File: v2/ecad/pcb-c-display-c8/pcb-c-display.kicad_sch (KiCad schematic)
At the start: 192 parts, among them Q1 AO3401A P-FET high side, Q2 2N7002, Q3 2N7002, Q4 2N7002, Q5 AO3401A P-FET: the e-paper's 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, Q6 Si1308EDL class N-FET (RDS un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, U1 PCA9555PW 0x22: LED sinks, li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, U2 PCA9555PW 0x23: LED sinks, th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, U3 RP2040 panel controller (USB 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, U4 W25Q16JVUXIQ 16 Mbit QSPI fla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, U5 TLV75533PDBV 3.3 V 500 mA LDO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, U6 USBLC6-2SC6, U7 USBLC6-2SC6, U8 USBLC6-2SC6, U9 74LVC1G34 non-inverting buffe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, Y1 12 MHz ABM8-272-T3 (3225): 1 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

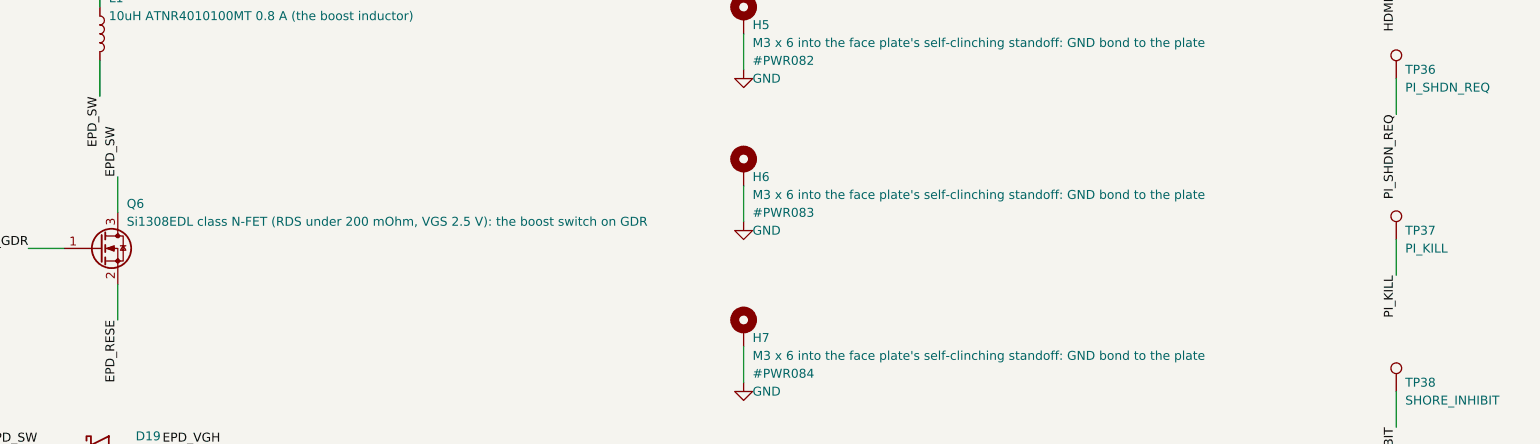
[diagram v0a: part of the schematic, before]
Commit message: chore(ecad): the phase directories' netlists brought current, and the contracts pass 42 of 42 [MESHSAT-862]
check_contracts read every board as MISSING because the netlist beside it in this tree was older than the
schematic beside it: B's by two days, C's by a day, D's and E's by the re-cuts of the 13th. A netlist older
than its schematic is not a netlist of that board, and the check is right to refuse it, so the cross-board
gate has been INCONCLUSIVE rather than passing for as long as those copies have been stale.

Fetched from the phase directories that generated them, schematic and netlist together. ALL CONTRACTS PASS,
42 of 42, the first reading of this gate on seven boards that all exist.
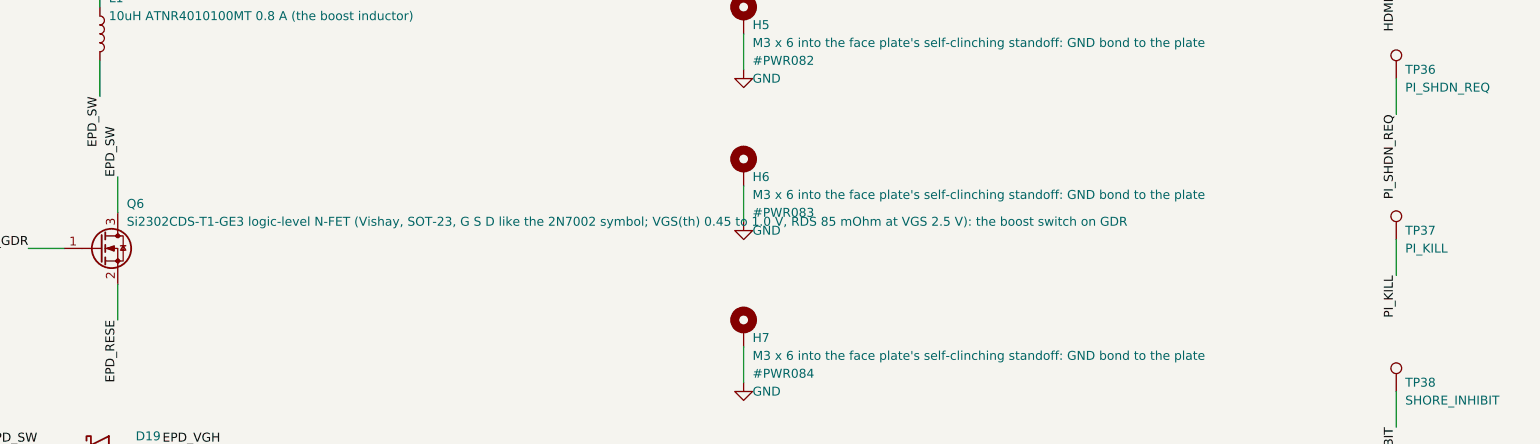
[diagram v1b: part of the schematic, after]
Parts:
- Q6: value Si1308EDL class N-FET (RDS under 200 mOhm, VGS 2.5 V): the boost switch on GDR -> Si2302CDS-T1-GE3 logic-level N-FET (Vishay, SOT-23, G S D like the 2N7002 symbol; VGS(th) 0.45 to 1.0 V, RDS 85 mOhm at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; LCSC C8545 -> C10488
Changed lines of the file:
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@@
 	(symbol (lib_id "Transistor_FET:2N7002") (at 500.38 222.25 0) (unit 1) (exclude_from_sim no) (in_bom yes) (on_board yes) (dnp no) (fields_autoplaced yes)
 		(property "Reference" "Q6" (at 504.19 215.90 0) (effects (font (size 1.27 1.27)) (justify left)))
-		(property "Value" "Si1308EDL class N-FET (RDS under 200 mOhm, VGS 2.5 V): the boost switch on GDR" (at 504.19 218.44 0) (effects (font (size 1.27 1.27)) (justify left)))
+		(property "Value" "Si2302CDS-T1-GE3 logic-level N-FET (Vishay, SOT-23, G S D like the 2N7002 symbol; VGS(th) 0.45 to 1.0 V, RDS 85 mOhm at VGS 2.5 V): the boost switch on GDR" (at 504.19 218.44 0) (effects (font (size 1.27 1.27)) (justify left)))
 		(property "Footprint" "Package_TO_SOT_SMD:SOT-23" (at 500.38 222.25 0) (effects (font (size 1.27 1.27)) (justify left) (hide yes)))
 		(property "Datasheet" "" (at 500.38 222.25 0) (effects (font (size 1.27 1.27)) (justify left) (hide yes)))
 		(property "Description" "" (at 500.38 222.25 0) (effects (font (size 1.27 1.27)) (justify left) (hide yes)))
-		(property "LCSC" "C8545" (at 500.38 222.25 0) (effects (font (size 1.27 1.27)) (justify left) (hide yes)))
+		(property "LCSC" "C10488" (at 500.38 222.25 0) (effects (font (size 1.27 1.27)) (justify left) (hide yes)))
 		(pin "1")
 		(pin "3")

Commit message: feat(c): C17 cut, the first C deliverable: 0 hard, 0 unrouted, check ALL PASS, 1 of 1 rails MET, netlist 852 of 852, verify_deliverable 36 of 36 [MESHSAT-862]
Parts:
- CAM_H1, CAM_H2: now left out of the parts list
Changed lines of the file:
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@@
 		(instances (project "pcb-c-display" (path "/d6380e1a-52de-5b28-8e34-f3cd11e930e3" (reference "#PWR075") (unit 1))))
 	)
-	(symbol (lib_id "Mechanical:MountingHole") (at 500.38 673.10 0) (unit 1) (exclude_from_sim no) (in_bom yes) (on_board yes) (dnp no) (fields_autoplaced yes)
+	(symbol (lib_id "Mechanical:MountingHole") (at 500.38 673.10 0) (unit 1) (exclude_from_sim no) (in_bom no) (on_board yes) (dnp no) (fields_autoplaced yes)
 		(property "Reference" "CAM_H1" (at 501.65 671.83 0) (effects (font (size 1.27 1.27)) (justify left)))
 		(property "Value" "M2 screw of the USB camera module (25 x 25 board, sheet owed) behind the plate's sealed window" (at 501.65 674.37 0) (effects (font (size 1.27 1.27)) (justify left)))
@@
 		(instances (project "pcb-c-display" (path "/d6380e1a-52de-5b28-8e34-f3cd11e930e3" (reference "CAM_H1") (unit 1))))
 	)
-	(symbol (lib_id "Mechanical:MountingHole") (at 500.38 695.96 0) (unit 1) (exclude_from_sim no) (in_bom yes) (on_board yes) (dnp no) (fields_autoplaced yes)
+	(symbol (lib_id "Mechanical:MountingHole") (at 500.38 695.96 0) (unit 1) (exclude_from_sim no) (in_bom no) (on_board yes) (dnp no) (fields_autoplaced yes)
 		(property "Reference" "CAM_H2" (at 501.65 694.69 0) (effects (font (size 1.27 1.27)) (justify left)))
 		(property "Value" "M2 screw of the USB camera module (25 x 25 board, sheet owed) behind the plate's sealed window" (at 501.65 697.23 0) (effects (font (size 1.27 1.27)) (justify left)))

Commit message: feat(ecad): readable schematics: a page engine draws every board as wired A3 pages of functional blocks (ICs as boxes with rails top and grounds bottom, passives on the pins they serve, decoupling rows, power symbols), proves the drawing's connectivity before writing, and the build cuts the sheet into A3 pages; all six netlists identical; the render scene puts the lit display on the glass and the monitor's rear block under it [MESHSAT-862]
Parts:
- removed C11: 100n, Capacitor_SMD:C_0603_1608Metric, symbol Device:C
- removed C21: 10n, Capacitor_SMD:C_0603_1608Metric, symbol Device:C
- removed C4: 1u, Capacitor_SMD:C_0603_1608Metric, symbol Device:C
- removed D11: 3 mm MSG white, sunlight viewable, LED_THT:LED_D3.0mm, symbol Device:LED
- removed D21: SS2040FL: pump -> VGL, Diode_SMD:D_SOD-123F, symbol Device:D_Schottky
- removed D4: 3 mm SOSACT red, sunlight viewable, LED_THT:LED_D3.0mm, symbol Device:LED
- removed H2, H4, H6, H8: M3 x 6 into the face plate's self-clinching stand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, meshsat:BackerScrew_M3_GND, symbol Mechanical:MountingHole_Pad
- removed R10: 10k, Resistor_SMD:R_0603_1608Metric, symbol Device:R
- removed R26, R33: 180R, Resistor_SMD:R_0603_1608Metric, symbol Device:R
- removed R3: 27R, Resistor_SMD:R_0603_1608Metric, symbol Device:R
- removed R39: 470R, Resistor_SMD:R_0603_1608Metric, symbol Device:R
- removed R44: 100R, Resistor_SMD:R_0603_1608Metric, symbol Device:R
- removed SW_LIGHT: LIGHTING DAY/NIGHT/BLACKOUT toggle DPDT ON-ON-ON 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, meshsat:ToggleBody_DPDT, symbol Connector_Generic:Conn_01x06
- removed U5: TLV75533PDBV 3.3 V 500 mA LDO for the controller,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, Package_TO_SOT_SMD:SOT-23-5, symbol Connector_Generic:Conn_01x05
- removed U9: 74LVC1G34 non-inverting buffer (2 A 4 Y): EMCON_H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, Package_TO_SOT_SMD:SOT-23-5, symbol Connector_Generic:Conn_01x05
- removed U_LIGHT: Vishay VEML7700 ambient light sensor (1 SCL 2 VDD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, meshsat:Vishay_VEML7700, symbol Connector_Generic:Conn_01x04
- added C25: 100n, Capacitor_SMD:C_0603_1608Metric, symbol Device:C
- added C3: 1u, Capacitor_SMD:C_0603_1608Metric, symbol Device:C
- added C34: 1u 25V, Capacitor_SMD:C_0603_1608Metric, symbol Device:C
- added C5: 15p NP0, Capacitor_SMD:C_0402_1005Metric, symbol Device:C
- added D14: 3 mm BAT3 green, sunlight viewable, LED_THT:LED_D3.0mm, symbol Device:LED
- added D9: 3 mm SHORE green, sunlight viewable, LED_THT:LED_D3.0mm, symbol Device:LED
- added FB2: ferrite 600R, Inductor_SMD:L_0603_1608Metric, symbol Device:L
- added Q1: AO3401A P-FET high side, Package_TO_SOT_SMD:SOT-23, symbol Transistor_FET:AO3401A
- added R20: 100k, Resistor_SMD:R_0603_1608Metric, symbol Device:R
- added R22: 300R, Resistor_SMD:R_0603_1608Metric, symbol Device:R
- added R28: 180R, Resistor_SMD:R_0603_1608Metric, symbol Device:R
- added SW_MAIN: MAIN PWR 19 mm momentary, green ring (to A22 J_MA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, meshsat:PanelSwitch_19mm, symbol Connector_Generic:Conn_01x04
- added TP20: SPARE8, TestPoint:TestPoint_Pad_D1.5mm, symbol Connector:TestPoint
- added TP25: EPD_BUSY, TestPoint:TestPoint_Pad_D1.5mm, symbol Connector:TestPoint
- added TP28: HB1, TestPoint:TestPoint_Pad_D1.5mm, symbol Connector:TestPoint
- added TP31: SLOT_EN1, TestPoint:TestPoint_Pad_D1.5mm, symbol Connector:TestPoint
- added TP34: HDMI_SEL1, TestPoint:TestPoint_Pad_D1.5mm, symbol Connector:TestPoint
- added U4: W25Q16JVUXIQ 16 Mbit QSPI flash (USON-8: 1 CS 2 D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, Package_SON:Winbond_USON-8-1EP_3x2mm_P0.5mm_EP0.2x1.6mm, symbol meshsat_ic:U4
- added U5: TLV75533PDBV 3.3 V 500 mA LDO for the controller,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, Package_TO_SOT_SMD:SOT-23-5, symbol meshsat_ic:U5
- added U_LIGHT: Vishay VEML7700 ambient light sensor (1 SCL 2 VDD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, meshsat:Vishay_VEML7700, symbol meshsat_ic:U_LIGHT
- C11: renamed from C5; value 15p NP0 -> 100n; footprint Capacitor_SMD:C_0402_1005Metric -> Capacitor_SMD:C_0603_1608Metric
- C21: renamed from R19; value 100R -> 10n; footprint Resistor_SMD:R_0603_1608Metric -> Capacitor_SMD:C_0603_1608Metric; symbol Device:R -> Device:C; LCSC C22775 -> C57112
- D11: renamed from R28; value 180R -> 3 mm MSG white, sunlight viewable; footprint Resistor_SMD:R_0603_1608Metric -> LED_THT:LED_D3.0mm; symbol Device:R -> Device:LED; LCSC C22828 -> (none)
- D21: renamed from C34; value 1u 25V -> SS2040FL: pump -> VGL; footprint Capacitor_SMD:C_0603_1608Metric -> Diode_SMD:D_SOD-123F; symbol Device:C -> Device:D_Schottky
- D4: renamed from R22; value 300R -> 3 mm SOSACT red, sunlight viewable; footprint Resistor_SMD:R_0603_1608Metric -> LED_THT:LED_D3.0mm; symbol Device:R -> Device:LED; LCSC C23025 -> (none)
- H2: renamed from TP25; value EPD_BUSY -> M3 x 6 into the face plate's self-clinching standoff: GND bond to the plate; footprint TestPoint:TestPoint_Pad_D1.5mm -> meshsat:BackerScrew_M3_GND; symbol Connector:TestPoint -> Mechanical:MountingHole_Pad; now in the parts list
- H4: renamed from TP28; value HB1 -> M3 x 6 into the face plate's self-clinching standoff: GND bond to the plate; footprint TestPoint:TestPoint_Pad_D1.5mm -> meshsat:BackerScrew_M3_GND; symbol Connector:TestPoint -> Mechanical:MountingHole_Pad; now in the parts list
- H6: renamed from TP31; value SLOT_EN1 -> M3 x 6 into the face plate's self-clinching standoff: GND bond to the plate; footprint TestPoint:TestPoint_Pad_D1.5mm -> meshsat:BackerScrew_M3_GND; symbol Connector:TestPoint -> Mechanical:MountingHole_Pad; now in the parts list
- H8: renamed from TP34; value HDMI_SEL1 -> M3 x 6 into the face plate's self-clinching standoff: GND bond to the plate; footprint TestPoint:TestPoint_Pad_D1.5mm -> meshsat:BackerScrew_M3_GND; symbol Connector:TestPoint -> Mechanical:MountingHole_Pad; now in the parts list
- R10: renamed from Q1; value AO3401A P-FET high side -> 10k; footprint Package_TO_SOT_SMD:SOT-23 -> Resistor_SMD:R_0603_1608Metric; symbol Transistor_FET:AO3401A -> Device:R; LCSC C15127 -> C25804
- R19: renamed from SW_MAIN; value MAIN PWR 19 mm momentary, green ring (to A22 J_MAINSW); C&K ATP19-SL1-603-B0SA-03G; silicone gasket washer under the be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 -> 100R; footprint meshsat:PanelSwitch_19mm -> Resistor_SMD:R_0603_1608Metric; symbol Connector_Generic:Conn_01x04 -> Device:R; LCSC (none) -> C22775
- R26: renamed from D9; value 3 mm SHORE green, sunlight viewable -> 180R; footprint LED_THT:LED_D3.0mm -> Resistor_SMD:R_0603_1608Metric; symbol Device:LED -> Device:R; LCSC (none) -> C22828
- R3: renamed from U4; value W25Q16JVUXIQ 16 Mbit QSPI flash (USON-8: 1 CS 2 DO/IO1 3 WP/IO2 4 GND 5 DI/IO0 6 CLK 7 HOLD/IO3 8 VCC, pad) -> 27R; footprint Package_SON:Winbond_USON-8-1EP_3x2mm_P0.5mm_EP0.2x1.6mm -> Resistor_SMD:R_0603_1608Metric; symbol Connector_Generic:Conn_01x09 -> Device:R; LCSC C2843335 -> (none)
- R33: renamed from D14; value 3 mm BAT3 green, sunlight viewable -> 180R; footprint LED_THT:LED_D3.0mm -> Resistor_SMD:R_0603_1608Metric; symbol Device:LED -> Device:R; LCSC (none) -> C22828
- R39: renamed from FB2; value ferrite 600R -> 470R; footprint Inductor_SMD:L_0603_1608Metric -> Resistor_SMD:R_0603_1608Metric; symbol Device:L -> Device:R; LCSC C1002 -> C23179
- R44: renamed from TP20; value SPARE8 -> 100R; footprint TestPoint:TestPoint_Pad_D1.5mm -> Resistor_SMD:R_0603_1608Metric; symbol Connector:TestPoint -> Device:R; LCSC (none) -> C22775; now in the parts list
- SW_LIGHT: renamed from R20; value 100k -> LIGHTING DAY/NIGHT/BLACKOUT toggle DPDT ON-ON-ON (pole 1: rail, pole 2: sense); NKK M2044SD3A01 on the D3 splashproof b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; footprint Resistor_SMD:R_0603_1608Metric -> meshsat:ToggleBody_DPDT; symbol Device:R -> Connector_Generic:Conn_01x06; LCSC C25803 -> (none)
- U9: renamed from C25; value 100n -> 74LVC1G34 non-inverting buffer (2 A 4 Y): EMCON_HW follows TX_INHIBIT_n; low = every transmitter inhibited (32.50 item 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; footprint Capacitor_SMD:C_0603_1608Metric -> Package_TO_SOT_SMD:SOT-23-5; symbol Device:C -> meshsat_ic:U9
- renumbered C3 to C4
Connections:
- net +3V3: now also C11.1, C4.1, R10.2, U9.5 (+3V3), C25.1, U4.8 (+3V3), U5.5 (+3V3), U_LIGHT.2 (+3V3); no longer R3.8 (Pin_8), U9.1
- net +5V: now also SW_LIGHT.2 (Pin_2), C3.1, U5.1 (+5V), U5.3 (+5V); no longer C4.1
- net BAT3_A: now also D14.2 (A)
- net BAT3_K: now also D14.1 (K); no longer R33.1 (K)
- net EMCON_HW: now also U9.4 (EMCON_HW)
- net EPD_BUSY: now also TP25.1; no longer H2.1
- net EPD_PUMP: now also D21.2 (A)
- net EPD_VDDD: now also C34.1; no longer D21.1
- net EPD_VGL: now also D21.1 (K)
- net GND: now also C21.2, H2.1, H4.1, H6.1, H8.1, SW_LIGHT.4 (Pin_4), U9.3 (GND), C25.2, C3.2, C34.2, C5.2, R20.2, SW_MAIN.4 (Pin_4), U4.4 (GND), U4.9 (GND), U5.2 (GND), U_LIGHT.3 (GND); no longer D21.2, R19.4 (Pin_4), R3.4 (Pin_4), R3.9 (Pin_9), SW_LIGHT.2, U9.2
- net HB1: now also TP28.1; no longer H4.1
- net HDMI_SEL1: now also TP34.1; no longer H8.1
- net LED_RAIL: now also R26.1, R33.1, Q1.3 (D), R22.1, R28.1; no longer D11.1, D4.1, R10.3 (D)
- net LED_RAIL_SW: now also R39.1, SW_LIGHT.1 (Pin_1), Q1.2 (S); no longer R10.2 (S)
- net LIGHT_DAY_n: now also SW_LIGHT.5 (Pin_5)
- net LIGHT_NIGHT_n: now also SW_LIGHT.6 (Pin_6)
- net LTE_A: now also R26.2
- net MAINRING_A: now also R39.2, SW_MAIN.3 (Pin_3); no longer R19.3 (Pin_3)
- net MAINSW_A: now also SW_MAIN.1 (Pin_1); no longer R19.1 (Pin_1)
- net MAINSW_B: now also FB2.1, SW_MAIN.2 (Pin_2); no longer R19.2 (Pin_2), R39.1
- net MAINSW_B2: now also FB2.2; no longer R39.2
- net MCAUT_A: now also R22.2; no longer D4.2
- net MSG_A: now also D11.2 (A)
- net MSG_K: now also D11.1 (K)
- net PANEL_PWM: now also R19.1; no longer C21.1
- net PWM1: now also R44.1
- net Q1_G: now also Q1.1 (G); no longer R10.1 (G)
- net Q2_G: now also R19.2, R20.1; no longer C21.2, SW_LIGHT.1
- net Q4_G: now also R44.2
- net QSPI_D0: now also U4.5 (QSPI_D0); no longer R3.5 (Pin_5)
- net QSPI_D1: now also U4.2 (QSPI_D1); no longer R3.2 (Pin_2)
- net QSPI_D2: now also U4.3 (QSPI_D2); no longer R3.3 (Pin_3)
- net QSPI_D3: now also U4.7 (QSPI_D3); no longer R3.7 (Pin_7)
- net QSPI_SCLK: now also U4.6 (QSPI_SCLK); no longer R3.6 (Pin_6)
- net QSPI_SS: now also U4.1 (QSPI_SS); no longer R3.1 (Pin_1)
- net SCL: now also U_LIGHT.1 (SCL)
- net SDA: now also U_LIGHT.4 (SDA)
- net SHORE_A: now also D9.2 (A), R28.2; no longer D11.2, R26.2 (A)
- net SHORE_K: now also D9.1 (K); no longer R26.1 (K)
- net SLOT_EN1: now also TP31.1; no longer H6.1
- net SOSACT_A: now also D4.2 (A)
- net SOSACT_K: now also D4.1 (K)
- net SPARE8: now also TP20.1; no longer R44.1
- net TEST_SW: now also C21.1
- net TX_INHIBIT_n: now also U9.2 (TX_INHIBIT_n)
- net USB_DM_R: now also R3.1
- net USB_PNL_N: now also R3.2
- net XIN: now also C5.1; no longer C11.1
- net ZEROIZE_HW: now also R10.1
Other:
- note added: "10uH"
- note added: "12 MHz ABM8-272-T3"
- note added: "1k"
- note added: "3 mm BAT1 amber"
- note added: "3 mm BAT2 green"
- note added: "3 mm BAT3 green"
- note added: "3 mm BAT4 green"
- note added: "3 mm BAT5 green"
- note added: "3 mm CHG white"
- note added: "3 mm GPS green"
- note added: "3 mm LTE green"
- note added: "3 mm MCAUT amber"
- note added: "3 mm MESH green"
- note added: "3 mm MSG white"
- note added: "3 mm MWARN red"
- note added: "3 mm SAT green"
- note added: "3 mm SHORE green"
- note added: "3 mm SOSACT red"
- note added: "3 mm TX red"
- note added: "74LVC1G34 non-inverting buffer"
- note added: "AO3401A P-FET"
- note added: "BOOTSEL"
- note added: "EMCON locking toggle"
- note added: "Hirose FH34SRJ-24S-0.5SH ZIF for t.."
- note added: "IP67 panel-mount sounder"
- note added: "LED RAIL, INDICATORS, TX LAMP, SWITCHES AND LEADS (continued)"
- note added: "LED RAIL, INDICATORS, TX LAMP, SWITCHES AND LEADS | E-PAPER ZIF AND THE PDi BOOST, SOUNDER, LIGHT SENSOR, CAMERA MOUNT | STANDOFF SCREWS (GND BOND), TEST POINTS, THE"
- note added: "LIGHTING DAY/NIGHT/BLACKOUT toggle.."
- note added: "M2 screw of the USB camera module"
- note added: "M3 x 6 into the face plate's self-.."
- note added: "MAIN PWR 19 mm momentary"
- note added: "MAIN button lead to A22 J_MAINSW"
- note added: "PANEL_ID strap"
- note added: "PCA9555PW 0x22"
- note added: "PCA9555PW 0x23"
- note added: "PCB-C CONTROL PANEL BACKER C17"
- note added: "PI 16 mm recessed momentary"
- note added: "PI button lead"
- note added: "RIBBON FROM B16, 5 V, 3.3 V LDO, USB AND BUS ESD, FLAGS | RP2040 PANEL CONTROLLER, FLASH, CRYSTAL, BOOTSEL, BUS PULL-UPS"
- note added: "RP2040 PANEL CONTROLLER, FLASH, CRYSTAL, BOOTSEL, BUS PULL-UPS (continued)"
- note added: "RP2040 PANEL CONTROLLER, FLASH, CRYSTAL, BOOTSEL, BUS PULL-UPS | EXPANDERS 0x22 / 0x23, MODE INPUTS, EMCON INVERTER, STRAPS | LED RAIL, INDICATORS, TX LAMP, SWITCHES"
- note added: "RP2040 panel controller"
- note added: "SOS locking toggle"
- note added: "SS2040FL"
- note added: "STANDOFF SCREWS (GND BOND), TEST POINTS, THE REST (continued)"
- note added: "Si2302CDS-T1-GE3 logic-level N-FET"
- note added: "TEST/ACK 16 mm momentary"
- note added: "TLV75533PDBV 3.3 V 500 mA LDO for.."
- note added: "U-174/U headset jack 1"
- note added: "U-174/U headset jack 2"
- note added: "Vishay VEML7700 ambient light sensor"
- note added: "W25Q16JVUXIQ 16 Mbit QSPI flash"
- note added: "ZEROIZE locking toggle"
- note added: "page 1 of 5 MeshSat field kit V2, CERN-OHL-S-2.0 PROTOTYPE, nothing built 2026-09-15"
- note added: "page 2 of 5 MeshSat field kit V2, CERN-OHL-S-2.0 PROTOTYPE, nothing built 2026-09-15"
- note added: "page 3 of 5 MeshSat field kit V2, CERN-OHL-S-2.0 PROTOTYPE, nothing built 2026-09-15"
- note added: "page 4 of 5 MeshSat field kit V2, CERN-OHL-S-2.0 PROTOTYPE, nothing built 2026-09-15"
- note added: "page 5 of 5 MeshSat field kit V2, CERN-OHL-S-2.0 PROTOTYPE, nothing built 2026-09-15"
- note added: "panel ribbon from B16 J_PANEL"
- note added: "status"
- moved on the sheet: C11, C4, H2, H4, H6, H8

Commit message: feat(ecad): the schematic pages draw every net that stays on a page as wires between its parts and mark every signal that leaves a page with the pages it goes to; B's shared area is sectioned by its generator headings; six netlists identical [MESHSAT-862]
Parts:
- removed C18, C38: 100n, Capacitor_SMD:C_0603_1608Metric, symbol Device:C
- removed C20: 10n, Capacitor_SMD:C_0603_1608Metric, symbol Device:C
- removed C34: 1u 25V, Capacitor_SMD:C_0603_1608Metric, symbol Device:C
- removed CAM_H2: M2 screw of the USB camera module (25 x 25 board,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, MountingHole:MountingHole_2.2mm_M2, symbol Mechanical:MountingHole
- removed D15: 3 mm BAT4 green, sunlight viewable, LED_THT:LED_D3.0mm, symbol Device:LED
- removed D19: SS2040FL: EPD_SW -> VGH, Diode_SMD:D_SOD-123F, symbol Device:D_Schottky
- removed FB1: ferrite 600R, Inductor_SMD:L_0603_1608Metric, symbol Device:L
- removed J_HSJ2: U-174/U headset jack 2 (Amphenol Nexus class, dra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, meshsat:PanelJack_17mm, symbol Mechanical:MountingHole
- removed Q2: 2N7002, Package_TO_SOT_SMD:SOT-23, symbol Transistor_FET:2N7002
- removed Q5: AO3401A P-FET: the e-paper's supply switch (EPD_P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, Package_TO_SOT_SMD:SOT-23, symbol Transistor_FET:AO3401A
- removed R27: 180R, Resistor_SMD:R_0603_1608Metric, symbol Device:R
- removed SW_MAIN: MAIN PWR 19 mm momentary, green ring (to A22 J_MA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, meshsat:PanelSwitch_19mm, symbol Connector_Generic:Conn_01x04
- removed TP1: SWCLK, TestPoint:TestPoint_Pad_D1.5mm, symbol Connector:TestPoint
- removed U_LIGHT: Vishay VEML7700 ambient light sensor (1 SCL 2 VDD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, meshsat:Vishay_VEML7700, symbol meshsat_ic:U_LIGHT
- added C27: 100n, Capacitor_SMD:C_0603_1608Metric, symbol Device:C
- added D14: 3 mm BAT3 green, sunlight viewable, LED_THT:LED_D3.0mm, symbol Device:LED
- added D17: BAT54 lamp-test tie, Diode_SMD:D_SOD-123, symbol Device:D_Schottky
- added R16, R42, R9: 10k, Resistor_SMD:R_0603_1608Metric, symbol Device:R
- added R26: 180R, Resistor_SMD:R_0603_1608Metric, symbol Device:R
- added R43: 0.47R 1%, Resistor_SMD:R_0603_1608Metric, symbol Device:R
- added SW_TEST: TEST/ACK 16 mm momentary, white ring; C&K ATP16-S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, meshsat:PanelSwitch_16mm, symbol Connector_Generic:Conn_01x04
- added TP13: SPARE1, TestPoint:TestPoint_Pad_D1.5mm, symbol Connector:TestPoint
- added TP19: SPARE7, TestPoint:TestPoint_Pad_D1.5mm, symbol Connector:TestPoint
- added TP31: SLOT_EN1, TestPoint:TestPoint_Pad_D1.5mm, symbol Connector:TestPoint
- added TP34: HDMI_SEL1, TestPoint:TestPoint_Pad_D1.5mm, symbol Connector:TestPoint
- added TP38: SHORE_INHIBIT, TestPoint:TestPoint_Pad_D1.5mm, symbol Connector:TestPoint
- added TP39: PIJ2_A, TestPoint:TestPoint_Pad_D1.5mm, symbol Connector:TestPoint
- C18: renamed from R9; value 10k -> 100n; footprint Resistor_SMD:R_0603_1608Metric -> Capacitor_SMD:C_0603_1608Metric; symbol Device:R -> Device:C; LCSC C25804 -> C14663
- C20: renamed from R26; value 180R -> 10n; footprint Resistor_SMD:R_0603_1608Metric -> Capacitor_SMD:C_0603_1608Metric; symbol Device:R -> Device:C; LCSC C22828 -> C57112
- C34: renamed from R43; value 0.47R 1% -> 1u 25V; footprint Resistor_SMD:R_0603_1608Metric -> Capacitor_SMD:C_0603_1608Metric; symbol Device:R -> Device:C
- C38: renamed from TP34; value HDMI_SEL1 -> 100n; footprint TestPoint:TestPoint_Pad_D1.5mm -> Capacitor_SMD:C_0603_1608Metric; symbol Connector:TestPoint -> Device:C; now in the parts list
- CAM_H2: renamed from TP38; value SHORE_INHIBIT -> M2 screw of the USB camera module (25 x 25 board, sheet owed) behind the plate's sealed window; footprint TestPoint:TestPoint_Pad_D1.5mm -> MountingHole:MountingHole_2.2mm_M2; symbol Connector:TestPoint -> Mechanical:MountingHole
- D15: renamed from D17; value BAT54 lamp-test tie -> 3 mm BAT4 green, sunlight viewable; footprint Diode_SMD:D_SOD-123 -> LED_THT:LED_D3.0mm; symbol Device:D_Schottky -> Device:LED; LCSC C7502705 -> (none)
- D19: renamed from TP19; value SPARE7 -> SS2040FL: EPD_SW -> VGH; footprint TestPoint:TestPoint_Pad_D1.5mm -> Diode_SMD:D_SOD-123F; symbol Connector:TestPoint -> Device:D_Schottky; now in the parts list
- FB1: renamed from R42; value 10k -> ferrite 600R; footprint Resistor_SMD:R_0603_1608Metric -> Inductor_SMD:L_0603_1608Metric; symbol Device:R -> Device:L; LCSC (none) -> C1002
- J_HSJ2: renamed from TP39; value PIJ2_A -> U-174/U headset jack 2 (Amphenol Nexus class, drawing owed): 17 mm hole through the backer, bushing nut below; its five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; footprint TestPoint:TestPoint_Pad_D1.5mm -> meshsat:PanelJack_17mm; symbol Connector:TestPoint -> Mechanical:MountingHole; now in the parts list
- Q2: renamed from SW_TEST; value TEST/ACK 16 mm momentary, white ring; C&K ATP16-SL1-203-M0SA-04G; silicone gasket washer under the bezel -> 2N7002; footprint meshsat:PanelSwitch_16mm -> Package_TO_SOT_SMD:SOT-23; symbol Connector_Generic:Conn_01x04 -> Transistor_FET:2N7002; LCSC (none) -> C8545
- Q5: renamed from TP13; value SPARE1 -> AO3401A P-FET: the e-paper's supply switch (EPD_PWR_n low = on); footprint TestPoint:TestPoint_Pad_D1.5mm -> Package_TO_SOT_SMD:SOT-23; symbol Connector:TestPoint -> Transistor_FET:AO3401A; LCSC (none) -> C15127; now in the parts list
- R27: renamed from D14; value 3 mm BAT3 green, sunlight viewable -> 180R; footprint LED_THT:LED_D3.0mm -> Resistor_SMD:R_0603_1608Metric; symbol Device:LED -> Device:R; LCSC (none) -> C22828
- SW_MAIN: renamed from C27; value 100n -> MAIN PWR 19 mm momentary, green ring (to A22 J_MAINSW); C&K ATP19-SL1-603-B0SA-03G; silicone gasket washer under the be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; footprint Capacitor_SMD:C_0603_1608Metric -> meshsat:PanelSwitch_19mm; symbol Device:C -> Connector_Generic:Conn_01x04; LCSC C14663 -> (none)
- TP1: renamed from R16; value 10k -> SWCLK; footprint Resistor_SMD:R_0603_1608Metric -> TestPoint:TestPoint_Pad_D1.5mm; symbol Device:R -> Connector:TestPoint; LCSC C25804 -> (none); now left out of the parts list
- U_LIGHT: renamed from TP31; value SLOT_EN1 -> Vishay VEML7700 ambient light sensor (1 SCL 2 VDD 3 GND 4 SDA), I2C 0x10; footprint TestPoint:TestPoint_Pad_D1.5mm -> meshsat:Vishay_VEML7700; symbol Connector:TestPoint -> meshsat_ic:U_LIGHT; LCSC (none) -> C504893; now in the parts list
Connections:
- net +3V3: now also C18.1, C38.1, Q5.2 (S), U_LIGHT.2 (+3V3), R16.2, R42.2, R9.2; no longer C18.2, FB1.2, TP1.2
- net BAT3_A: now also D14.2 (A); no longer R27.2 (A)
- net BAT3_K: now also D14.1 (K); no longer R27.1 (K)
- net BAT4_A: now also D15.2 (A)
- net BAT4_K: now also D15.1 (K)
- net EPD_PWR_n: now also Q5.1 (G), R42.1; no longer FB1.1
- net EPD_RESE: now also R43.1; no longer C34.1
- net EPD_SW: now also D19.1 (K)
- net EPD_VCC: now also Q5.3 (D)
- net EPD_VDDD: now also C34.1
- net EPD_VGH: now also D19.2 (A)
- net GND: now also C18.2, C20.2, C38.2, SW_MAIN.4 (Pin_4), U_LIGHT.3 (GND), R43.2, SW_TEST.2 (Pin_2), SW_TEST.4 (Pin_4); no longer Q2.4 (Pin_4)
- net GPS_A: now also R27.2
- net HDMI_SEL1: now also TP34.1; no longer C38.1
- net LED_RAIL: now also R27.1, R26.1; no longer C20.1
- net LTE_A: now also R26.2; no longer C20.2
- net MAINRING_A: now also SW_MAIN.3 (Pin_3)
- net MAINSW_A: now also FB1.1, SW_MAIN.1 (Pin_1)
- net MAINSW_A2: now also FB1.2
- net MAINSW_B: now also SW_MAIN.2 (Pin_2)
- net PANEL_ID: now also R16.1; no longer TP1.1
- net PIJ2_A: now also TP39.1; no longer J_HSJ2.1
- net PIJ2_A2: now also C27.1; no longer SW_MAIN.1
- net PIJ2_B2: now also C27.2; no longer SW_MAIN.2
- net Q2_D: now also Q2.3 (D)
- net Q2_G: now also Q2.1 (G)
- net SCL: now also U_LIGHT.1 (SCL)
- net SDA: now also U_LIGHT.4 (SDA)
- net SHORE_INHIBIT: now also TP38.1; no longer CAM_H2.1
- net SLOT_EN1: now also TP31.1; no longer U_LIGHT.1
- net SOS_SW: now also R9.1; no longer C18.1
- net SPARE1: now also TP13.1; no longer Q5.1
- net SPARE7: now also TP19.1; no longer D19.1
- net SWCLK: now also TP1.1
- net TESTRING_A: now also SW_TEST.3 (Pin_3); no longer Q2.3 (Pin_3)
- net TEST_SW: now also SW_TEST.1 (Pin_1); no longer Q2.1 (Pin_1)
- net TX_K: now also D17.2 (A); no longer D15.2 (A)
- net TX_LAMPTEST: now also D17.1 (K); no longer D15.1 (K)
- net ZEROIZE_HW: now also C20.1
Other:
- note added: "LED RAIL, INDICATORS, TX LAMP, SWITCHES AND LEADS | E-PAPER ZIF AND THE PDi BOOST, SOUNDER, LIGHT SENSOR, CAMERA MOUNT"
- note added: "p1"
- note added: "p1,2"
- note added: "p1,2,3"
- note added: "p1,2,4"
- note added: "p1,2,5"
- note added: "p1,3"
- note added: "p1,3,4"
- note added: "p1,4"
- note added: "p1,4,5"
- note added: "p1,5"
- note added: "p2"
- note added: "p2,3,4"
- note added: "p2,4"
- note added: "p2,4,5"
- note added: "p2,5"
- note added: "p3"
- note added: "p3,4"
- note added: "p4"
- note added: "p4,5"
- note added: "p5"
- note removed: "LED RAIL, INDICATORS, TX LAMP, SWITCHES AND LEADS | E-PAPER ZIF AND THE PDi BOOST, SOUNDER, LIGHT SENSOR, CAMERA MOUNT | STANDOFF SCREWS (GND BOND), TEST POINTS, THE"
- note removed: "STANDOFF SCREWS (GND BOND), TEST POINTS, THE REST (continued)"
- moved on the sheet: C10, C11, C12, C16, C7, C8, C9
